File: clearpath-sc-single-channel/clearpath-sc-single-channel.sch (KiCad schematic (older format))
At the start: 38 parts

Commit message: Added serial and regulator ICs
FT230 series USB TTL IC added, 12 and 5V linear regs added.
Reorganised some content and fixed label directions.
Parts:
- added C? (x2): 100NF_X7R_1608M, CAPC1608*, symbol 100NF_X7R_1608M
- added C? (x2): 1UF_X7R_2012M, CAPC2012*, symbol 1UF_X7R_2012M
- added C? (x2): 1UF_X7R_3216M, Applidyne_Capacitor:CAPC3216X135N, symbol 1UF_X7R_3216M
- added R? (x2): 22R_1608M, RESC1608*, symbol 22R_1608M
- added R?: 470K_1608M, RESC1608*, symbol 470K_1608M
- added R?: 768R_1608M, RESC1608*, symbol 768R_1608M
- added R? (x2): 240R_1608M, RESC1608*, symbol 240R_1608M
- added R?: 2K2_1608M, RESC1608*, symbol 2K2_1608M
- added R?: 750R_1608M, RESC1608*, symbol 750R_1608M
- added U?: FT230XS-R, symbol FT230XS-R
- added U? (x2): LM317LCPK, SOT89*, symbol LM317LCPK
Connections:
- net labels added: USB_3V3OUT, USB_VDD
- wire segments 146 -> 205
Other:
- note added: ""R1""
- note added: ""R2""
- note added: "12.7V calculated"
- note added: "12V Regulator"
- note added: "5.16V calculated"
- note added: "5V Regulator"
- note added: "Provides 'driverless' USB serial adaptor for Windows/OSX/*nix.\nCan be configured over USB with official FTDI FT_prog tool"
- note added: "The SC4-Hub from Teknic uses nice isolated DC-DC supplies and assumes 24V in.\nThis board is slightly simpler and input filtering will be reduced slightly.\nRegulation is designed to support 13-24V input power and 'should' handle 30V."
- note added: "USB ESD Device"
- note added: "Vout = 1.25V * ( 1 + R2/R1)"
- note removed: "470k"
- note removed: "768R"
- note removed: "FT230XS-R\n5V capable SSOP16 IC"
- moved on the sheet: C?, D?, F?, P?, R?, U?E, U?F

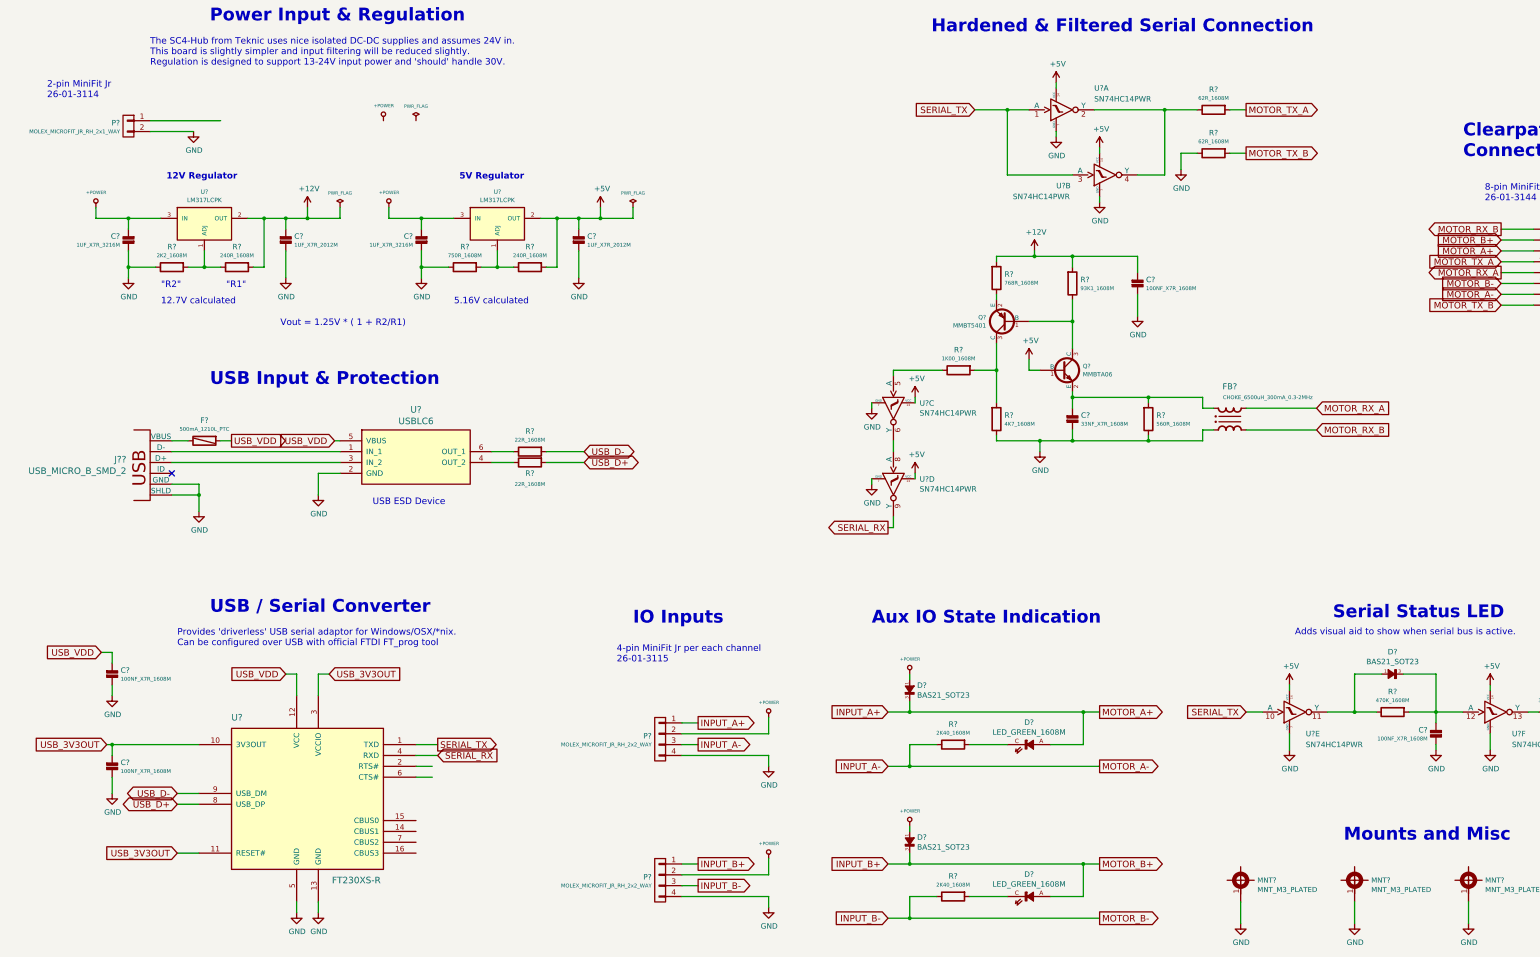
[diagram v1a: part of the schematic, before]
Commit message: Regulator and input circuits finished.
Added pdf of current sch and updated readme.
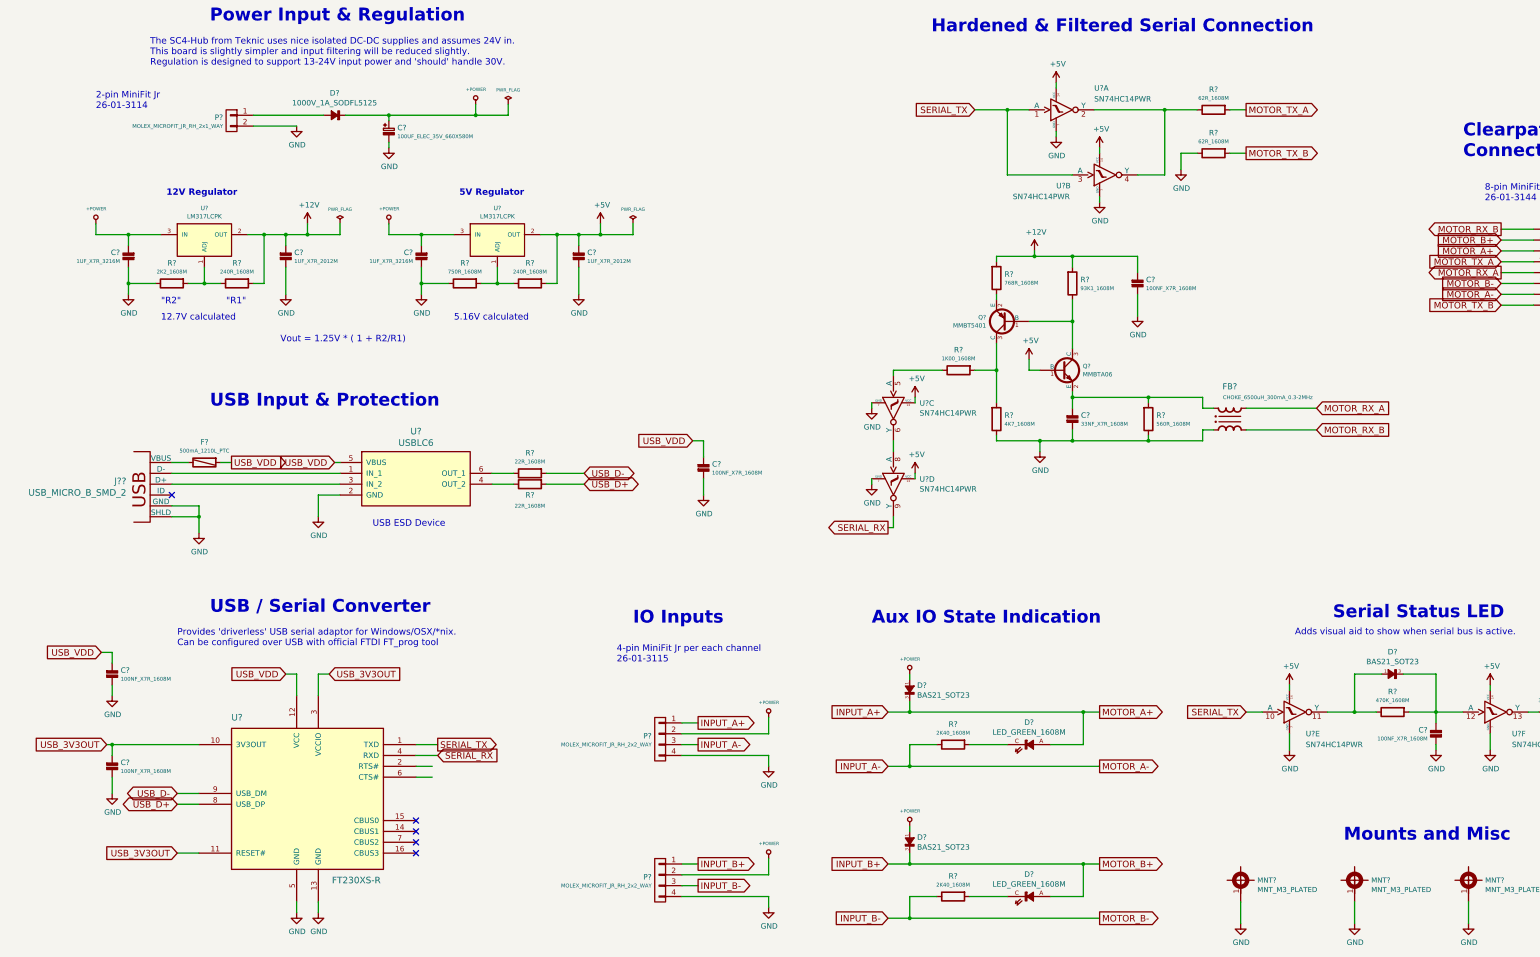
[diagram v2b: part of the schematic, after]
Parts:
- added C?: 100NF_X7R_1608M, CAPC1608*, symbol 100NF_X7R_1608M
- added C?: 100UF_ELEC_35V_660X580M, CAPAE660X580DD180L260*, symbol 100UF_ELEC_35V_660X580M
- added D?: 1000V_1A_SODFL5125, Applidyne_SOD:SODFL5125X250N, symbol 1000V_1A_SODFL5125
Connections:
- net +POWER: now also C?.1, D?.C
- net GND: now also C?.2, C?.2
- net USB_VDD: now also C?.1
- net at P?.1 (P1): now also D?.A
- no-connect marks 1 -> 5
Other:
- moved on the sheet: C?, F?, J??, P?, R?, U?

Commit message: Annotated and DRC checks
Fixed some DRC warnings.
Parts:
- gave numbers to parts that had none: 53
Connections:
- net SERIAL_RX: now also U5.4 (Y); no longer U5.9 (Y)
- net SERIAL_TX: now also U5.5 (A), U5.8 (A); no longer U5.1 (A), U5.3 (A)
- net at R9.2: now also U5.1 (A); no longer U5.5 (A)
- new net: R14.2, U5.6 (Y), U5.9 (Y)
- new net: U5.2 (Y), U5.3 (A)
- no-connect marks 5 -> 7
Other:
- moved on the sheet: F1, U3

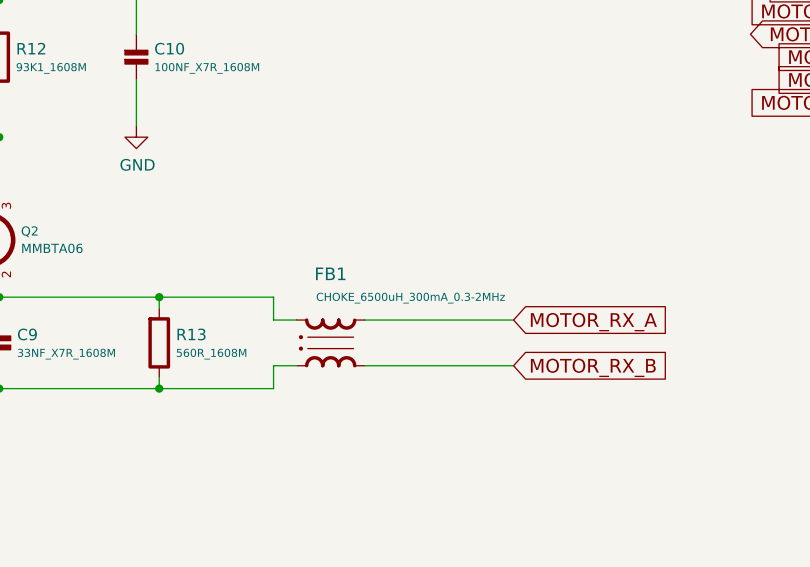
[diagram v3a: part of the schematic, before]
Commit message: Full footprint association, netlist generation
DRC passes with no errors, ready for layout.
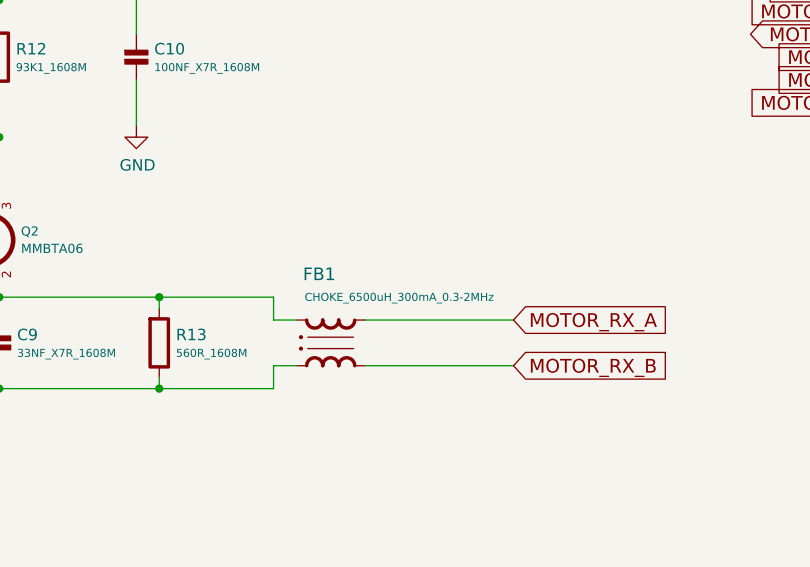
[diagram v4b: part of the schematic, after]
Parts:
- C1, C10, C11, C2, C8, C9: footprint CAPC1608* -> Applidyne_Capacitor:CAPC1608X90N
- C4, C7: footprint CAPC2012* -> Applidyne_Capacitor:CAPC2012X110N
- C5: footprint CAPAE660X580DD180L260* -> Applidyne_Capacitor:CAPAE660X580DD180L260N
- D2, D3, D6, Q1, Q2: footprint SOT95P240X110-3L16* -> Applidyne_SOT:SOT95P240X110-3L16N
- D4, D5, D7: footprint (none) -> Applidyne_LED:LEDC1608X80L40N
- FB1: footprint (none) -> Applidyne_Inductor:SRF0905
- MNT1, MNT2, MNT3, MNT4: footprint MTGP650H330 -> Applidyne_Mount:MTGP650H330
- P1: footprint (none) -> Applidyne_Connector_Molex:Molex_MiniFit-JR-5569-02A2_2x01x4.20mm_Angled
- P2, P3: footprint (none) -> Applidyne_Connector_Molex:Molex_MiniFit-JR-5569-04A2_2x02x4.20mm_Angled
- P4: footprint (none) -> Applidyne_Connector_Molex:Molex_MiniFit-JR-5569-08A2_2x04x4.20mm_Angled
- R1, R10, R11, R13, R14, R15, R16, R17, R2, R3, R4, R5, R6, R7, R8, R9: footprint RESC1608* -> Applidyne_Resistor:RESC1608X50N
- U1, U4: footprint SOT89* -> Applidyne_SOT:SOT89N
- U2: footprint (none) -> Applidyne_SOP:SOP16P65_500X640X120L62X24N
- U3: footprint (none) -> Applidyne_SOT:SOT95P280X145-6L50N
